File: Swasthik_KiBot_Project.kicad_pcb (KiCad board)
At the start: 2 copper layers, 30.5 x 15.4 mm, 5 parts, among them J1 Screw_Terminal_01x02, J2 Screw_Terminal_01x02, U1 NCP1117-3.3_SOT223

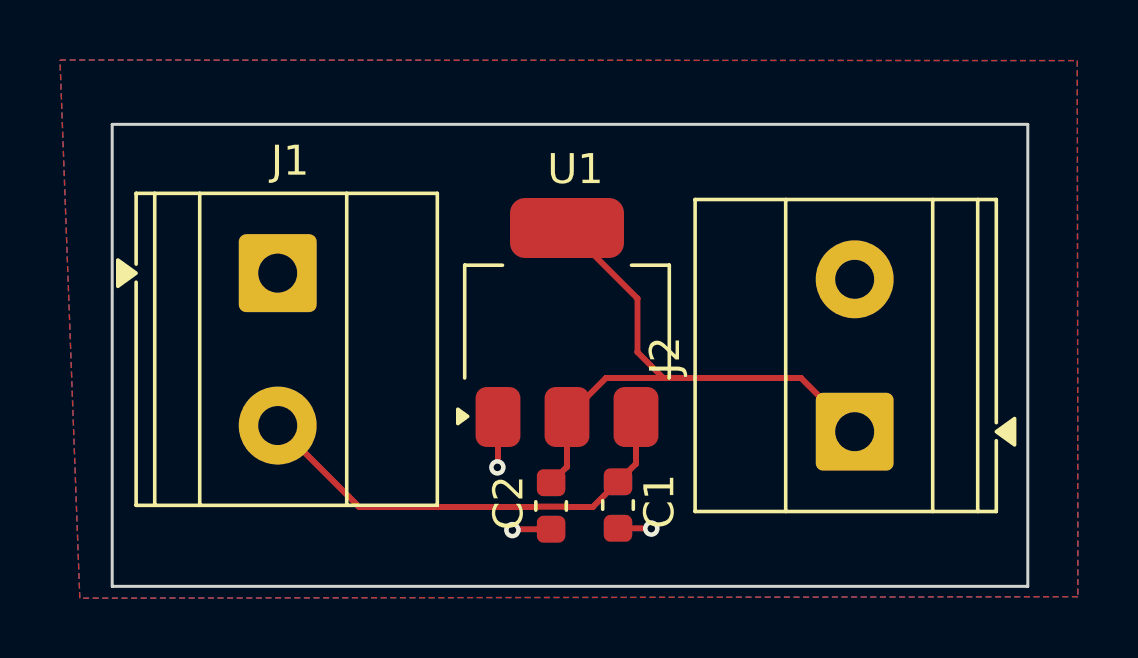
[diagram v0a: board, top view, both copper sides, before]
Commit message: Add LDO Schematic and Layout
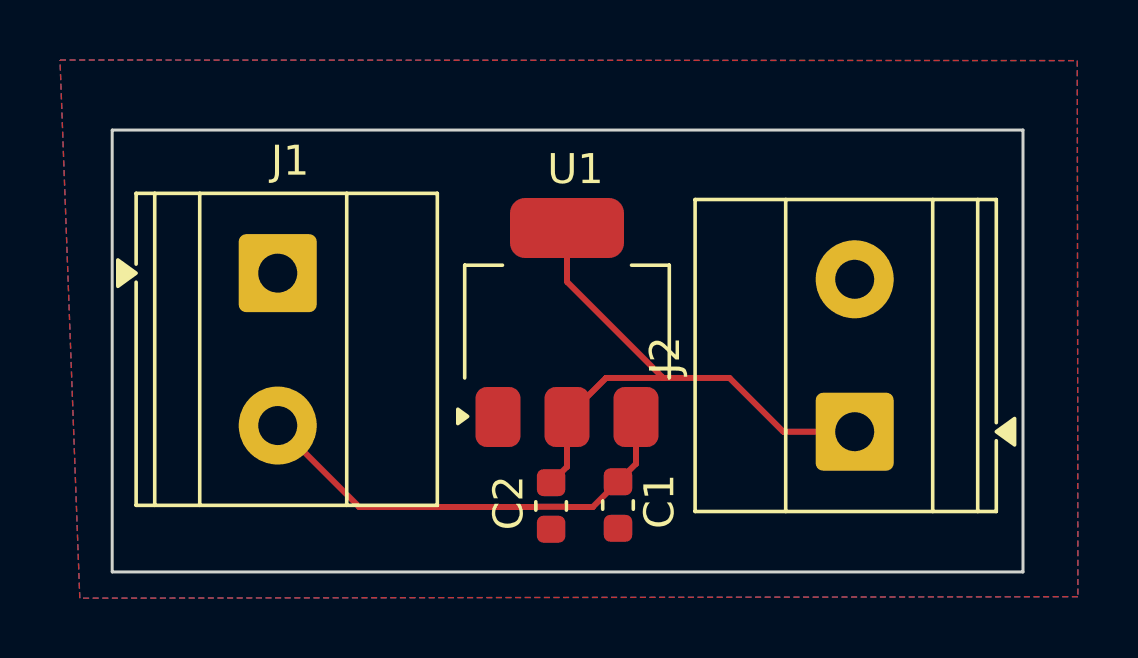
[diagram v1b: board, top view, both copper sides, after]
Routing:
- net GND: track 4.10 -> 0.00 mm, vias 3 -> 0
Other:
- board size 30.5 x 15.4 mm -> 30.4 x 14.7 mm
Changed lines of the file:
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@@
 	)
 	(gr_rect
-		(start 196.39 65.815)
-		(end 226.91 81.215)
+		(start 196.39 66.005)
+		(end 226.75 80.735)
 		(stroke
 			(width 0.1)
@@
 	)
 	(segment
-		(start 213.9 71.62)
-		(end 213.9 73.41)
-		(width 0.2)
-		(layer "F.Cu")
-		(net 2)
-	)
-	(segment
-		(start 214.759 74.269)
-		(end 214.78 74.269)
-		(width 0.2)
-		(layer "F.Cu")
-		(net 2)
-	)
-	(segment
 		(start 214.78 74.269)
 		(end 212.851 74.269)
@@
 	)
 	(segment
-		(start 221.14 76.06)
-		(end 219.349 74.269)
-		(width 0.2)
-		(layer "F.Cu")
-		(net 2)
-	)
-	(segment
 		(start 211.55 69.27)
-		(end 213.9 71.62)
+		(end 211.55 71.06)
 		(width 0.2)
 		(layer "F.Cu")
@@
 	)
 	(segment
-		(start 213.9 73.41)
+		(start 211.55 71.06)
 		(end 214.759 74.269)
 		(width 0.2)
@@
 	)
 	(segment
-		(start 219.349 74.269)
+		(start 214.759 74.269)
 		(end 214.78 74.269)
 		(width 0.2)
@@
 	)
 	(segment
-		(start 212.851 74.269)
-		(end 211.55 75.57)
+		(start 216.969 74.269)
+		(end 214.78 74.269)
 		(width 0.2)
 		(layer "F.Cu")
@@
 	)
 	(segment
-		(start 211.55 75.57)
-		(end 211.55 77.23)
+		(start 218.76 76.06)
+		(end 216.969 74.269)
 		(width 0.2)
 		(layer "F.Cu")
@@
 	)
 	(segment
-		(start 211.02 79.31)
-		(end 209.76 79.31)
-		(width 0.2)
-		(layer "F.Cu")
-		(net 3)
-	)
-	(segment
-		(start 209.25 75.57)
-		(end 209.25 77.23)
-		(width 0.2)
-		(layer "F.Cu")
-		(net 3)
-	)
-	(segment
-		(start 214.35 79.28)
-		(end 214.36 79.29)
-		(width 0.2)
-		(layer "F.Cu")
-		(net 3)
-	)
-	(segment
-		(start 209.76 79.31)
-		(end 209.73 79.34)
+		(start 212.851 74.269)
+		(end 211.55 75.57)
 		(width 0.2)
 		(layer "F.Cu")
-		(net 3)
+		(net 2)
 	)
 	(segment
-		(start 209.25 77.23)
-		(end 209.23 77.25)
+		(start 211.55 75.57)
+		(end 211.55 77.23)
 		(width 0.2)
 		(layer "F.Cu")
-		(net 3)
+		(net 2)
 	)
 	(segment
-		(start 213.25 79.28)
-		(end 214.35 79.28)
+		(start 221.14 76.06)
+		(end 218.76 76.06)
 		(width 0.2)
 		(layer "F.Cu")
-		(net 3)
-	)
-	(via
-		(at 209.73 79.34)
-		(size 0.55)
-		(drill 0.25)
-		(layers "F.Cu" "B.Cu")
-		(net 3)
-	)
-	(via
-		(at 214.36 79.29)
-		(size 0.55)
-		(drill 0.25)
-		(layers "F.Cu" "B.Cu")
-		(net 3)
-	)
-	(via
-		(at 209.23 77.25)
-		(size 0.55)
-		(drill 0.25)
-		(layers "F.Cu" "B.Cu")
-		(net 3)
+		(net 2)
 	)
 	(zone

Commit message: Update layout
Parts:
- moved J2 0.36 mm to (221.0, 75.7)
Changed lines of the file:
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@@
 	(footprint "TerminalBlock_Phoenix:TerminalBlock_Phoenix_MKDS-1,5-2-5.08_1x02_P5.08mm_Horizontal"
 		(layer "F.Cu")
-		(at 221.14 76.06 90)
+		(at 221.03 75.72 90)
 		(descr "Terminal Block Phoenix MKDS-1,5-2-5.08, 2 pins, pitch 5.08mm, size 10.2x9.8mm, drill diameter 1.3mm, pad diameter 2.6mm, http://www.farnell.com/datasheets/100425.pdf, script-generated using https://gitlab.com/kicad/libraries/kicad-footprint-generator/-/tree/master/scripts/TerminalBlock_Phoenix")
 		(tags "THT Terminal Block Phoenix MKDS-1,5-2-5.08 pitch 5.08mm size 10.2x9.8mm drill 1.3mm pad 2.6mm")
 		(property "Reference" "J2"
-			(at 2.54 -6.32 90)
+			(at 9.08 -0.48 180)
 			(layer "F.SilkS")
 			(effects
@@
 		(tags "CMS SOT")
 		(property "Reference" "U1"
-			(at 5.11 0.28 180)
+			(at 5.44 -0.18 180)
 			(layer "F.SilkS")
 			(effects
@@
 	)
 	(segment
+		(start 220.8 75.72)
+		(end 218.42 75.72)
+		(width 0.2)
+		(layer "F.Cu")
+		(net 2)
+	)
+	(segment
 		(start 214.78 74.269)
 		(end 212.851 74.269)
@@
 	)
 	(segment
+		(start 216.969 74.269)
+		(end 214.78 74.269)
+		(width 0.2)
+		(layer "F.Cu")
+		(net 2)
+	)
+	(segment
 		(start 211.55 69.27)
 		(end 211.55 71.06)
@@
 	)
 	(segment
-		(start 216.969 74.269)
-		(end 214.78 74.269)
-		(width 0.2)
-		(layer "F.Cu")
-		(net 2)
-	)
-	(segment
-		(start 218.76 76.06)
-		(end 216.969 74.269)
+		(start 221.14 76.06)
+		(end 220.8 75.72)
 		(width 0.2)
 		(layer "F.Cu")
@@
 	)
 	(segment
-		(start 211.55 75.57)
-		(end 211.55 77.23)
+		(start 218.42 75.72)
+		(end 216.969 74.269)
 		(width 0.2)
 		(layer "F.Cu")
@@
 	)
 	(segment
-		(start 221.14 76.06)
-		(end 218.76 76.06)
+		(start 211.55 75.57)
+		(end 211.55 77.23)
 		(width 0.2)
 		(layer "F.Cu")
